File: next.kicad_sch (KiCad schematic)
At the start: 183 parts, among them J1 USB_mini_micro_B, K0:0 KEYSW, K0:1 KEYSW, K0:10 KEYSW, K0:11 KEYSW, K0:12 KEYSW, K0:13 KEYSW, K0:14 KEYSW, K0:15 KEYSW, K0:16 KEYSW, K0:2 KEYSW, K0:3 KEYSW, K0:3_1 KEYSW, K0:4 KEYSW, K0:5 KEYSW, K0:6 KEYSW, K0:7 KEYSW, K0:8 KEYSW, K0:9 KEYSW, K1:0 KEYSW, K1:1 KEYSW, K1:10 KEYSW, K1:11 KEYSW, K1:12 KEYSW, K1:13 KEYSW, K1:14 KEYSW, K1:15 KEYSW, K1:16 KEYSW, K1:2 KEYSW, K1:3 KEYSW, K1:4 KEYSW, K1:5 KEYSW, K1:6 KEYSW, K1:7 KEYSW, K1:8 KEYSW, K1:9 KEYSW, K2:0 KEYSW, K2:1 KEYSW, K2:10 KEYSW, K2:11 KEYSW, K2:12 KEYSW, K2:13 KEYSW, K2:14 KEYSW, K2:15 KEYSW, K2:16 KEYSW, K2:2 KEYSW, K2:3 KEYSW, K2:4 KEYSW, K2:5 KEYSW, K2:6 KEYSW, K2:7 KEYSW, K2:8 KEYSW, K2:9 KEYSW, K3:0 KEYSW, K3:1 KEYSW, K3:10 KEYSW, K3:11 KEYSW, K3:12 KEYSW, K3:13 KEYSW, K3:14 KEYSW, K3:15 KEYSW, K3:16 KEYSW, K3:2 KEYSW, K3:3 KEYSW, K3:3_1 KEYSW, K3:4 KEYSW, K3:5 KEYSW, K3:6 KEYSW, K3:7 KEYSW, K3:8 KEYSW, K3:9 KEYSW, K4:0 KEYSW, K4:0_1 KEYSW, K4:1 KEYSW, K4:14 KEYSW, K4:15 KEYSW, K4:16 KEYSW, K4:1_1 KEYSW, K4:2 KEYSW, K4:2_1 KEYSW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

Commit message: Update Axial_Diode Footprint
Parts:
- C1, C2: value 22pF -> 22p
- C3: value 1uF -> 1u
- C4: value 4.7uF -> 4.7u
- C5, C6, C7, C8: value 0.1uF -> 0.1u
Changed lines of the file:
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@@
       (effects (font (size 1.27 1.27)) (justify left))
     )
-    (property "Value" "22pF" (id 1) (at 184.15 57.15 0)
+    (property "Value" "22p" (id 1) (at 184.15 57.15 0)
       (effects (font (size 1.27 1.27)) (justify left))
     )
@@
       (effects (font (size 1.27 1.27)) (justify left))
     )
-    (property "Value" "22pF" (id 1) (at 193.04 57.15 0)
+    (property "Value" "22p" (id 1) (at 193.04 57.15 0)
       (effects (font (size 1.27 1.27)) (justify left))
     )
@@
       (effects (font (size 1.27 1.27)) (justify left))
     )
-    (property "Value" "0.1uF" (id 1) (at 130.175 49.53 0)
+    (property "Value" "0.1u" (id 1) (at 130.175 49.53 0)
       (effects (font (size 1.27 1.27)) (justify left))
     )
@@
       (effects (font (size 1.27 1.27)) (justify left))
     )
-    (property "Value" "0.1uF" (id 1) (at 137.795 49.53 0)
+    (property "Value" "0.1u" (id 1) (at 137.795 49.53 0)
       (effects (font (size 1.27 1.27)) (justify left))
     )
@@
       (effects (font (size 1.27 1.27)) (justify left))
     )
-    (property "Value" "0.1uF" (id 1) (at 145.415 49.53 0)
+    (property "Value" "0.1u" (id 1) (at 145.415 49.53 0)
       (effects (font (size 1.27 1.27)) (justify left))
     )
@@
       (effects (font (size 1.27 1.27)) (justify left))
     )
-    (property "Value" "0.1uF" (id 1) (at 153.035 49.53 0)
+    (property "Value" "0.1u" (id 1) (at 153.035 49.53 0)
       (effects (font (size 1.27 1.27)) (justify left))
     )
@@
       (effects (font (size 1.27 1.27)) (justify left))
     )
-    (property "Value" "1uF" (id 1) (at 214.63 80.645 0)
+    (property "Value" "1u" (id 1) (at 214.63 80.645 0)
       (effects (font (size 1.27 1.27)) (justify left))
     )
@@
       (effects (font (size 1.27 1.27)) (justify left))
     )
-    (property "Value" "4.7uF" (id 1) (at 119.38 49.53 0)
+    (property "Value" "4.7u" (id 1) (at 119.38 49.53 0)
       (effects (font (size 1.27 1.27)) (justify left))
     )
@@
     )
     (path "/00000000-0000-0000-0000-00005b6b239d"
-      (reference "C1") (unit 1) (value "22pF") (footprint "Capacitor_SMD:C_0805_2012Metric")
+      (reference "C1") (unit 1) (value "22p") (footprint "Capacitor_SMD:C_0805_2012Metric")
     )
     (path "/00000000-0000-0000-0000-00005b6b25fd"
-      (reference "C2") (unit 1) (value "22pF") (footprint "Capacitor_SMD:C_0805_2012Metric")
+      (reference "C2") (unit 1) (value "22p") (footprint "Capacitor_SMD:C_0805_2012Metric")
     )
     (path "/00000000-0000-0000-0000-00005b740dcd"
-      (reference "C3") (unit 1) (value "1uF") (footprint "Capacitor_SMD:C_0805_2012Metric")
+      (reference "C3") (unit 1) (value "1u") (footprint "Capacitor_SMD:C_0805_2012Metric")
     )
     (path "/00000000-0000-0000-0000-00005b9519e4"
-      (reference "C4") (unit 1) (value "4.7uF") (footprint "Capacitor_SMD:C_0805_2012Metric")
+      (reference "C4") (unit 1) (value "4.7u") (footprint "Capacitor_SMD:C_0805_2012Metric")
     )
     (path "/00000000-0000-0000-0000-00005b6c6eb5"
-      (reference "C5") (unit 1) (value "0.1uF") (footprint "Capacitor_SMD:C_0805_2012Metric")
+      (reference "C5") (unit 1) (value "0.1u") (footprint "Capacitor_SMD:C_0805_2012Metric")
     )
     (path "/00000000-0000-0000-0000-00005b6c9cc0"
-      (reference "C6") (unit 1) (value "0.1uF") (footprint "Capacitor_SMD:C_0805_2012Metric")
+      (reference "C6") (unit 1) (value "0.1u") (footprint "Capacitor_SMD:C_0805_2012Metric")
     )
     (path "/00000000-0000-0000-0000-00005b6c9ee6"
-      (reference "C7") (unit 1) (value "0.1uF") (footprint "Capacitor_SMD:C_0805_2012Metric")
+      (reference "C7") (unit 1) (value "0.1u") (footprint "Capacitor_SMD:C_0805_2012Metric")
     )
     (path "/00000000-0000-0000-0000-00005b6ca267"
-      (reference "C8") (unit 1) (value "0.1uF") (footprint "Capacitor_SMD:C_0805_2012Metric")
+      (reference "C8") (unit 1) (value "0.1u") (footprint "Capacitor_SMD:C_0805_2012Metric")
     )
     (path "/00000000-0000-0000-0000-0000597efb38"

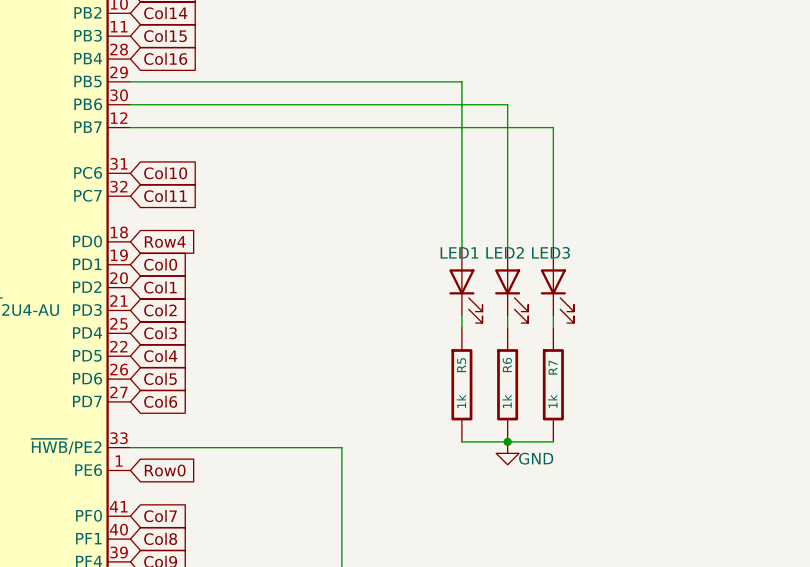
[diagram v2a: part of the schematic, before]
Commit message: Added LED opttion
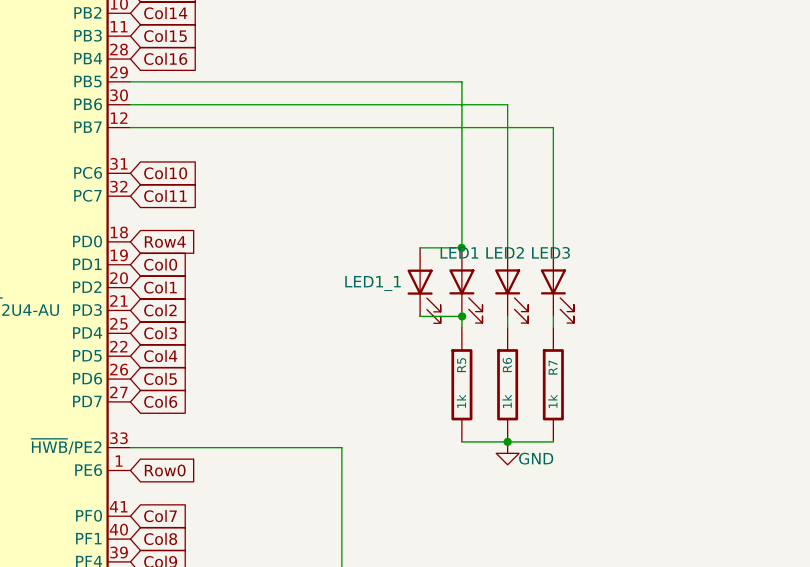
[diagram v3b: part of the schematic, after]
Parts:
- added LED1_1: LED, LED_THT:LED_D3.0mm, symbol Device:LED
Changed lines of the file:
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@@
   (junction (at 197.485 160.02) (diameter 0) (color 0 0 0 0)
   )
+  (junction (at 286.3596 66.7004) (diameter 0) (color 0 0 0 0)
+  )
   (junction (at 158.115 213.36) (diameter 0) (color 0 0 0 0)
   )
@@
   (junction (at 179.705 198.12) (diameter 0) (color 0 0 0 0)
   )
+  (junction (at 286.4104 74.3204) (diameter 0) (color 0 0 0 0)
+  )
   (junction (at 352.425 198.12) (diameter 0) (color 0 0 0 0)
   )
@@
     (stroke (width 0) (type default) (color 0 0 0 0))
   )
+  (wire (pts (xy 281.7368 74.3204) (xy 286.4104 74.3204))
+    (stroke (width 0) (type default) (color 0 0 0 0))
+  )
   (wire (pts (xy 219.075 160.02) (xy 219.075 175.26))
     (stroke (width 0) (type default) (color 0 0 0 0))
@@
     (stroke (width 0) (type default) (color 0 0 0 0))
   )
+  (wire (pts (xy 281.7368 66.7004) (xy 286.3596 66.7004))
+    (stroke (width 0) (type default) (color 0 0 0 0))
+  )
   (wire (pts (xy 287.655 190.5) (xy 290.195 190.5))
     (stroke (width 0) (type default) (color 0 0 0 0))
@@
     (pin "1")
   )
+  (symbol (lib_id "Device:LED") (at 281.7368 70.5104 90) (unit 1)
+    (in_bom yes) (on_board yes)
+    (property "Reference" "LED1_1" (id 0) (at 273.2532 70.5104 90)
+      (effects (font (size 1.27 1.27)) (justify right))
+    )
+    (property "Value" "LED" (id 1) (at 279.8318 67.9704 90)
+      (effects (font (size 1.27 1.27)) (justify right) hide)
+    )
+    (property "Footprint" "LED_THT:LED_D3.0mm" (id 2) (at 281.7368 70.5104 0)
+      (effects (font (size 1.27 1.27)) hide)
+    )
+    (property "Datasheet" "~" (id 3) (at 281.7368 70.5104 0)
+      (effects (font (size 1.27 1.27)) hide)
+    )
+    (pin "1")
+    (pin "2")
+  )
   (sheet_instances
     (path "/" (page "1"))
@@
       (reference "LED1") (unit 1) (value "LED") (footprint "LED_THT:LED_D3.0mm")
     )
+    (path "/8e1de856-3650-44fc-bdbc-9b70d85e955b"
+      (reference "LED1_1") (unit 1) (value "LED") (footprint "LED_THT:LED_D3.0mm")
+    )
     (path "/00000000-0000-0000-0000-000061bd1a30"

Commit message: Update diodes
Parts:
- D0:8, D0:9, D1:8, D1:9, D2:8, D2:9, D3:8, D3:9: footprint Keyboard_Footprints:Diode_123_Axial -> Diode_SMD:D_SOD-123
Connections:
- net at LED1.1 (K), R5.1: now also LED1_1.1 (K)
- net at LED1.2 (A), U1.29 (PB5): now also LED1_1.2 (A)
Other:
- moved on the sheet: LED1, LED2, LED3, R5, R6, R7

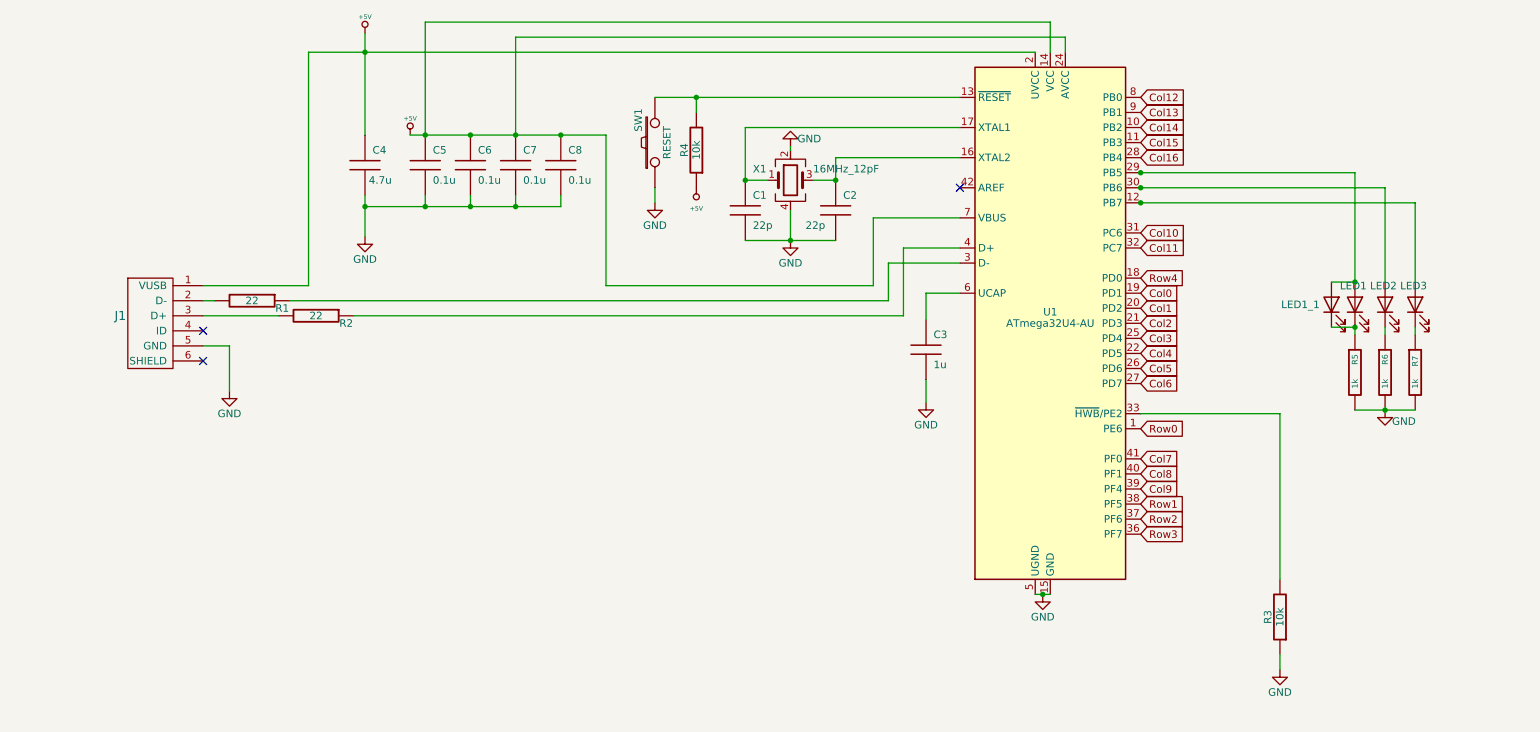
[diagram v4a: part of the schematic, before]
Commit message: Extend USB port mount
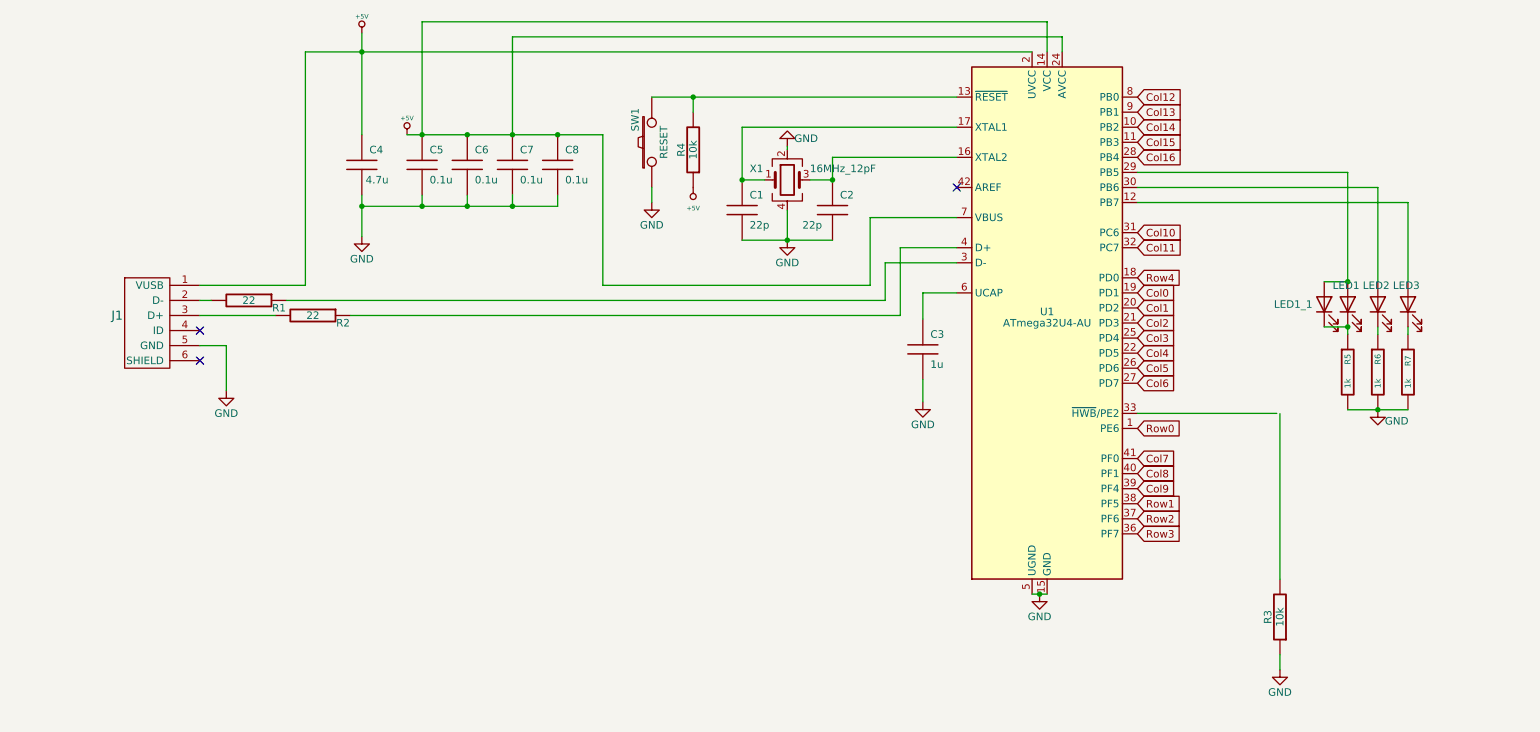
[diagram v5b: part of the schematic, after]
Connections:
- net at R3.2: no longer U1.33 (~{HWB}/PE2)
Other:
- moved on the sheet: C1, C2, C3, C4, C5, C6, C7, C8, J1, LED1, LED1_1, LED2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
